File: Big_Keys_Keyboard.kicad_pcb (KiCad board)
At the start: 2 copper layers, 9 parts, among them U1 MX1A-11NN, U2 MX1A-11NN, U3 MX1A-11NN, U4 MX1A-11NN

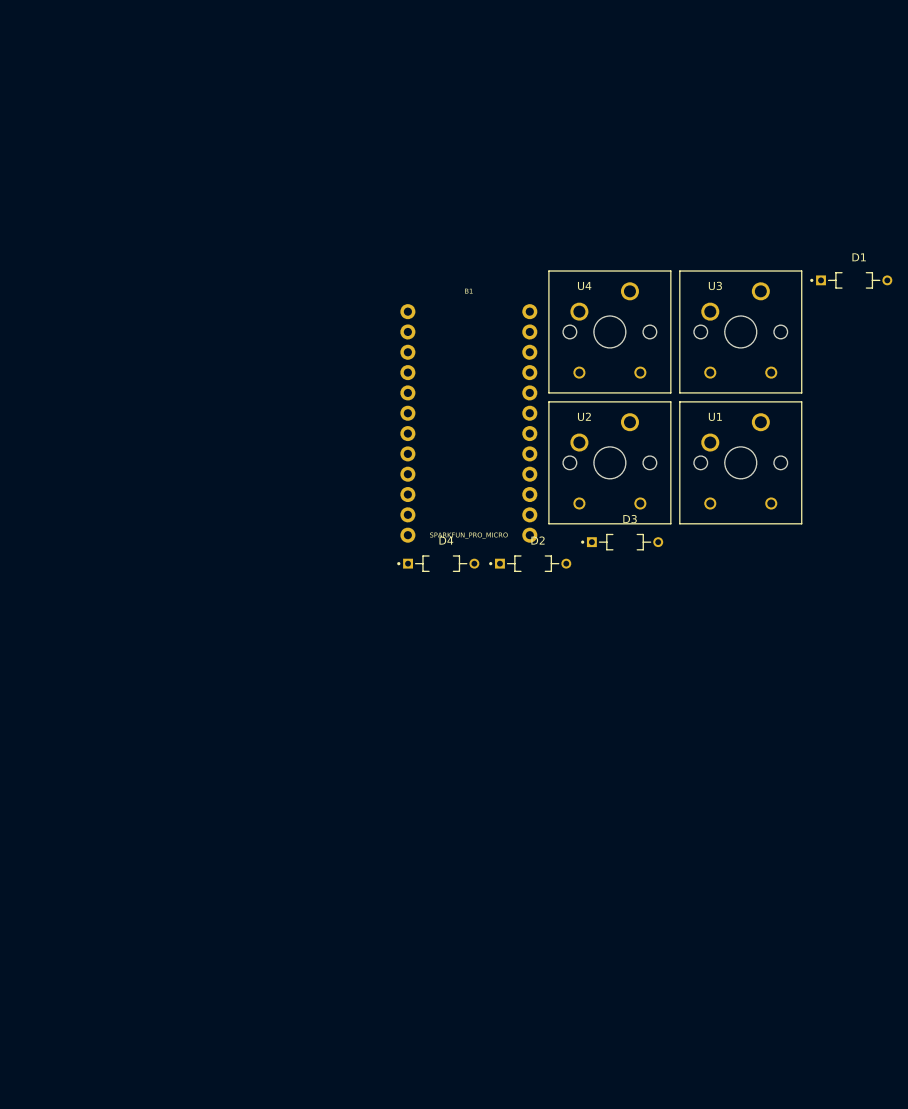
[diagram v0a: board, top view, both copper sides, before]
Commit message: keyboard routes connected in the PCB
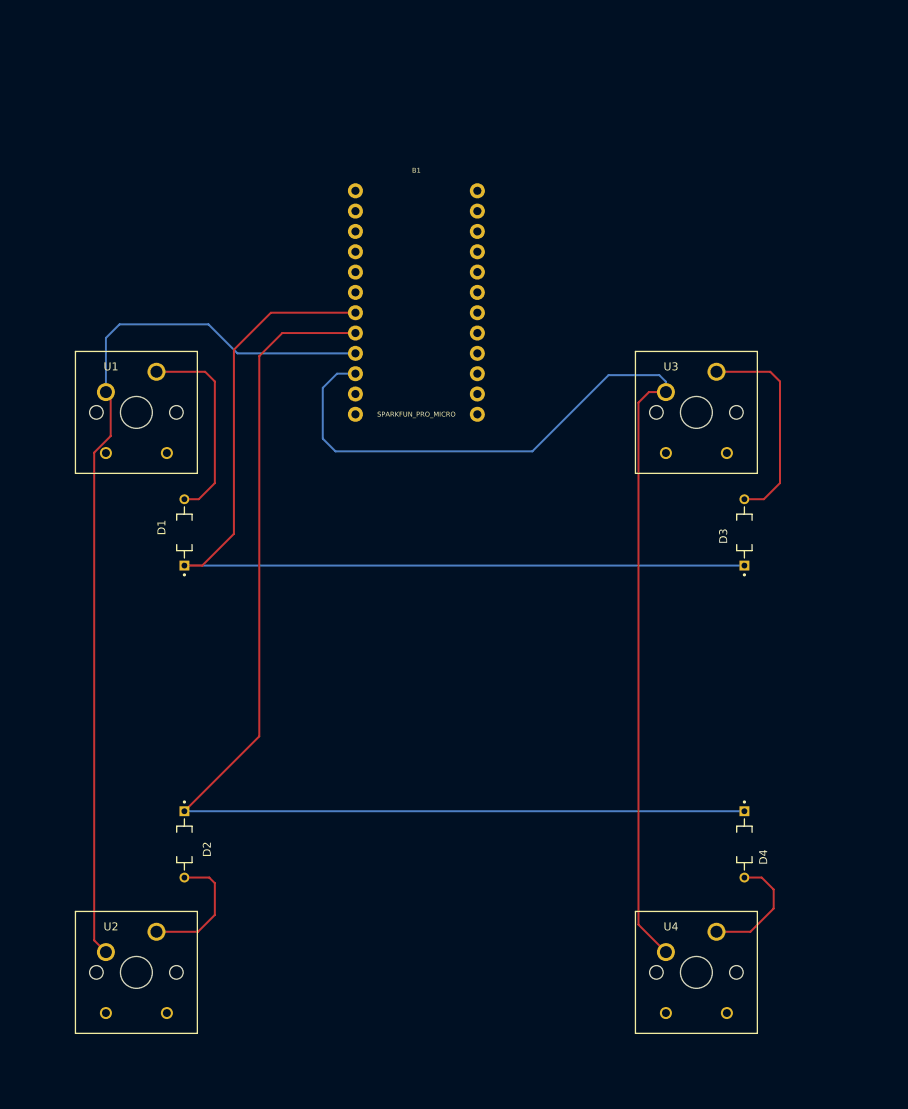
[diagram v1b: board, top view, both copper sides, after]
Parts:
- moved D1 89.5 mm to (97.0, 103.0), turned to 90 degrees
- moved U2 86.9 mm to (91.0, 158.0)
- moved U4 80.8 mm to (161.0, 158.0)
- moved U1 75.8 mm to (91.0, 88.0)
- moved D2 56.0 mm to (97.0, 142.0), turned to -90 degrees
- moved D4 51.6 mm to (167.0, 142.0), turned to -90 degrees
- moved B1 16.5 mm to (126.0, 73.0)
- moved D3 15.0 mm to (167.0, 103.0), turned to 90 degrees
- moved U3 11.5 mm to (161.0, 88.0)
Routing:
- net ROW2: track 0.00 -> 144.0 mm
- net COL2: track 0.00 -> 134.4 mm
- net ROW1: track 0.00 -> 118.0 mm
- net COL1: track 0.00 -> 111.9 mm
- net Net-(D3-PadA): track 0.00 -> 26.4 mm
- net Net-(D1-PadA): track 0.00 -> 25.1 mm
- net Net-(D2-PadA): track 0.00 -> 16.2 mm
- net Net-(D4-PadA): track 0.00 -> 15.0 mm

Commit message: basic pcb for a 4 keyed board ready
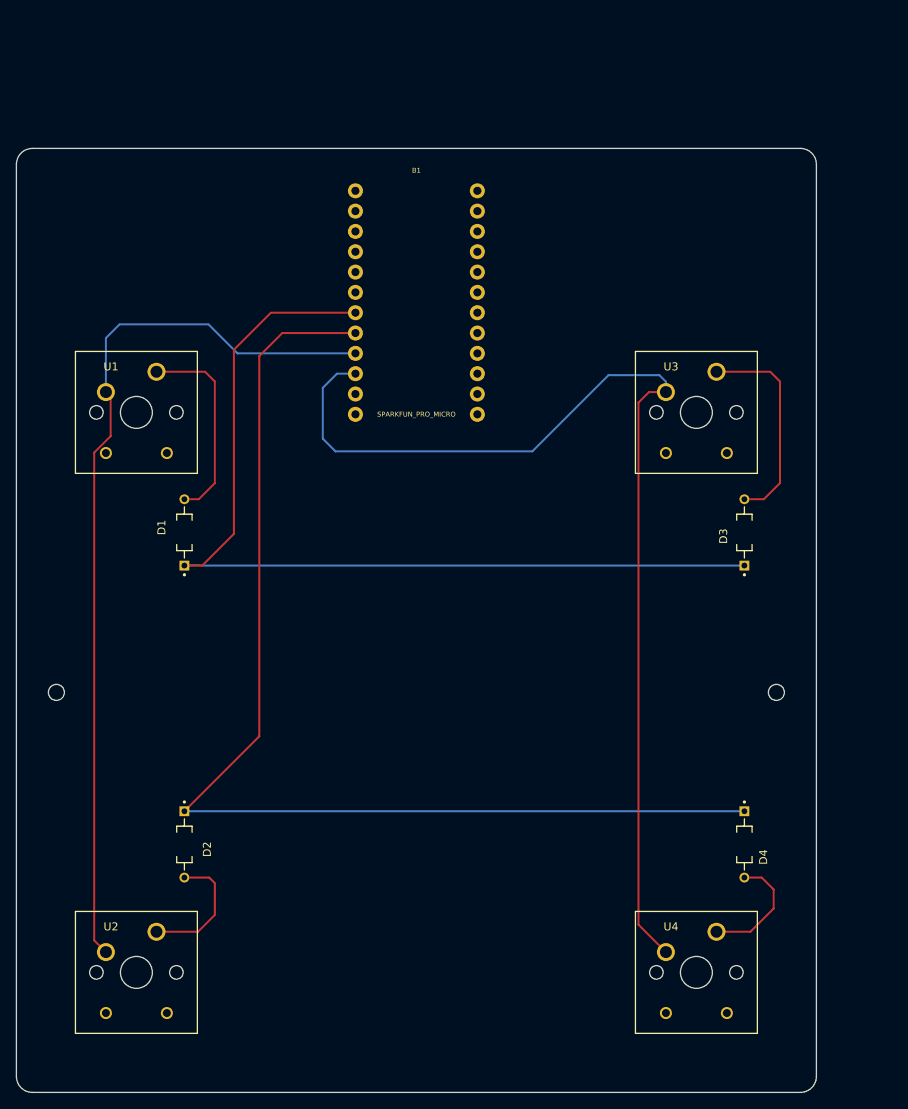
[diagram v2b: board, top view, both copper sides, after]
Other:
- board outline added: 100 x 118 mm
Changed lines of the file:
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@@
       (net 8 "ROW2") (pintype "passive"))
   )
+  (gr_line (start 176 57) (end 176 171) (layer "Edge.Cuts") (width 0.1))
+  (gr_line (start 174 173) (end 78 173) (layer "Edge.Cuts") (width 0.1))
+  (gr_circle (center 81 123) (end 82 123) (layer "Edge.Cuts") (width 0.15) (fill none))
+  (gr_arc (start 76 57) (mid 76.585786 55.585786) (end 78 55) (layer "Edge.Cuts") (width 0.1))
+  (gr_line (start 78 55) (end 174 55) (layer "Edge.Cuts") (width 0.1))
+  (gr_arc (start 176 171) (mid 175.414214 172.414214) (end 174 173) (layer "Edge.Cuts") (width 0.1))
+  (gr_arc (start 78 173) (mid 76.585786 172.414214) (end 76 171) (layer "Edge.Cuts") (width 0.1))
+  (gr_line (start 76 171) (end 76 57) (layer "Edge.Cuts") (width 0.1))
+  (gr_circle (center 171 123) (end 172 123) (layer "Edge.Cuts") (width 0.15) (fill none))
+  (gr_arc (start 174 55) (mid 175.414214 55.585786) (end 176 57) (layer "Edge.Cuts") (width 0.1))
   (segment (start 107.81625 75.54) (end 103.1875 80.16875) (width 0.25) (layer "F.Cu") (net 7))
   (segment (start 103.1875 80.16875) (end 103.1875 103.1875) (width 0.25) (layer "F.Cu") (net 7))
-  (segment (start 118.38 75.54) (end 107.81625 75.54) (width 0.25) (layer "F.Cu") (net 7))
+  (segment (start 118.38 75.54) (end 107.81625 75.54) (width 0.254) (layer "F.Cu") (net 7))
   (segment (start 103.1875 103.1875) (end 99.229 107.146) (width 0.25) (layer "F.Cu") (net 7))
   (segment (start 99.229 107.146) (end 97 107.146) (width 0.25) (layer "F.Cu") (net 7))
-  (segment (start 97 107.146) (end 167 107.146) (width 0.25) (layer "B.Cu") (net 7))
+  (segment (start 97 107.146) (end 167 107.146) (width 0.254) (layer "B.Cu") (net 7))
   (segment (start 106.3625 80.9625) (end 106.3625 128.4915) (width 0.25) (layer "F.Cu") (net 8))
   (segment (start 109.245 78.08) (end 106.3625 80.9625) (width 0.25) (layer "F.Cu") (net 8))
   (segment (start 106.3625 128.4915) (end 97 137.854) (width 0.25) (layer "F.Cu") (net 8))
-  (segment (start 118.38 78.08) (end 109.245 78.08) (width 0.25) (layer "F.Cu") (net 8))
-  (segment (start 97 137.854) (end 167 137.854) (width 0.25) (layer "B.Cu") (net 8))
+  (segment (start 118.38 78.08) (end 109.245 78.08) (width 0.254) (layer "F.Cu") (net 8))
+  (segment (start 97 137.854) (end 167 137.854) (width 0.254) (layer "B.Cu") (net 8))
   (segment (start 87.782717 90.961346) (end 85.725 93.019063) (width 0.25) (layer "F.Cu") (net 9))
   (segment (start 87.782717 86.052717) (end 87.782717 90.961346) (width 0.25) (layer "F.Cu") (net 9))
@@
   (segment (start 85.725 93.019063) (end 85.725 153.995) (width 0.25) (layer "F.Cu") (net 9))
   (segment (start 118.38 80.62) (end 103.63875 80.62) (width 0.25) (layer "B.Cu") (net 9))
-  (segment (start 100.0125 76.99375) (end 88.9 76.99375) (width 0.25) (layer "B.Cu") (net 9))
+  (segment (start 100.0125 76.99375) (end 88.9 76.99375) (width 0.254) (layer "B.Cu") (net 9))
   (segment (start 103.63875 80.62) (end 100.0125 76.99375) (width 0.25) (layer "B.Cu") (net 9))
   (segment (start 88.9 76.99375) (end 87.19 78.70375) (width 0.25) (layer "B.Cu") (net 9))
@@
   (segment (start 140.49375 92.86875) (end 150.01875 83.34375) (width 0.25) (layer "B.Cu") (net 10))
   (segment (start 116.07125 83.16) (end 114.3 84.93125) (width 0.25) (layer "B.Cu") (net 10))
-  (segment (start 99.58875 82.92) (end 100.80625 84.1375) (width 0.25) (layer "F.Cu") (net 25))
+  (segment (start 99.58875 82.92) (end 100.80625 84.1375) (width 0.254) (layer "F.Cu") (net 25))
   (segment (start 100.80625 84.1375) (end 100.80625 96.8375) (width 0.25) (layer "F.Cu") (net 25))
   (segment (start 93.51 82.92) (end 99.58875 82.92) (width 0.25) (layer "F.Cu") (net 25))
   (segment (start 100.80625 96.8375) (end 98.78975 98.854) (width 0.25) (layer "F.Cu") (net 25))
   (segment (start 98.78975 98.854) (end 97 98.854) (width 0.25) (layer "F.Cu") (net 25))
-  (segment (start 100.80625 150.8125) (end 100.80625 146.84375) (width 0.25) (layer "F.Cu") (net 26))
+  (segment (start 100.80625 150.8125) (end 100.80625 146.84375) (width 0.254) (layer "F.Cu") (net 26))
   (segment (start 98.69875 152.92) (end 100.80625 150.8125) (width 0.25) (layer "F.Cu") (net 26))
   (segment (start 93.51 152.92) (end 98.69875 152.92) (width 0.25) (layer "F.Cu") (net 26))
@@
   (segment (start 171.45 84.1375) (end 171.45 96.8375) (width 0.25) (layer "F.Cu") (net 27))
   (segment (start 163.51 82.92) (end 170.2325 82.92) (width 0.25) (layer "F.Cu") (net 27))
-  (segment (start 170.2325 82.92) (end 171.45 84.1375) (width 0.25) (layer "F.Cu") (net 27))
+  (segment (start 170.2325 82.92) (end 171.45 84.1375) (width 0.254) (layer "F.Cu") (net 27))
   (segment (start 167.755 152.92) (end 170.65625 150.01875) (width 0.25) (layer "F.Cu") (net 28))
   (segment (start 169.16475 146.146) (end 167 146.146) (width 0.25) (layer "F.Cu") (net 28))

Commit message: keyboard with all connections done, lack of i2c
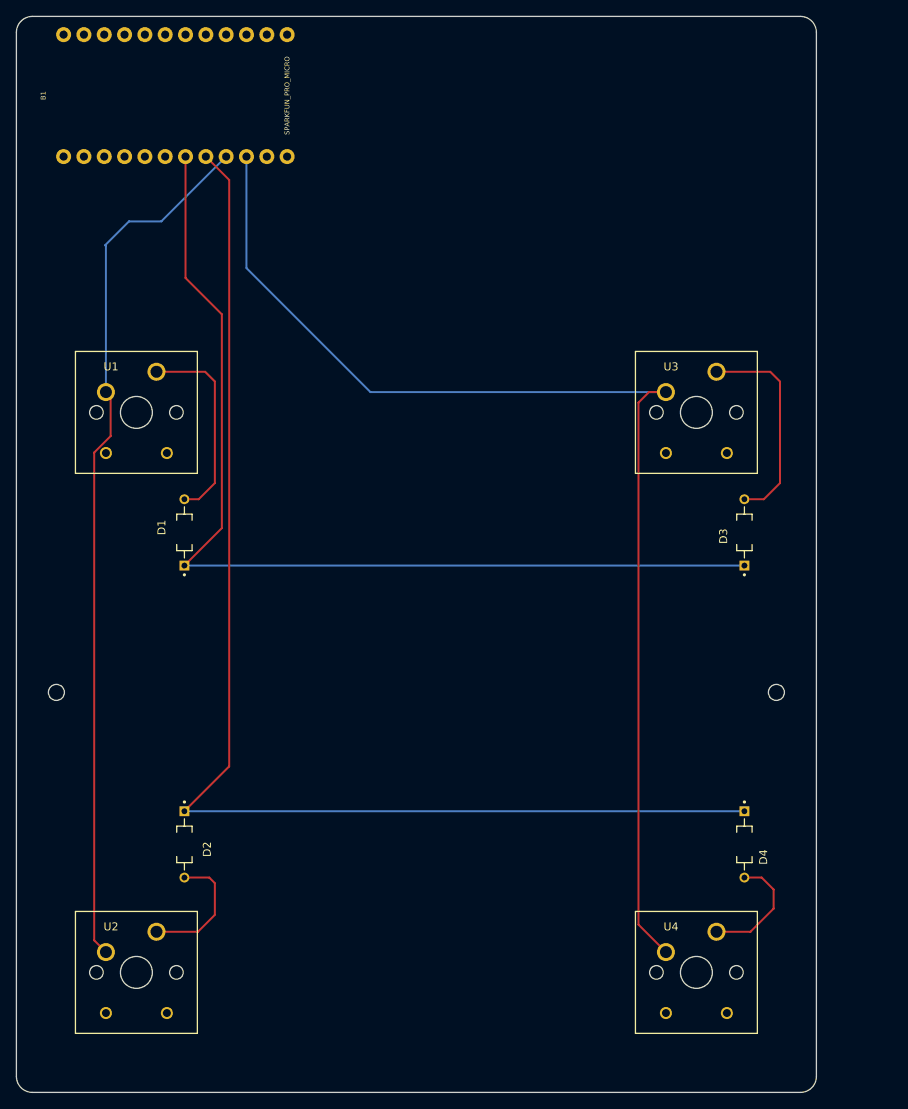
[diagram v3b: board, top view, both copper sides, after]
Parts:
- moved B1 39.9 mm to (94.6, 48.4), turned to 90 degrees
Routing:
- net COL2: track 134.4 -> 146.9 mm
- net ROW2: track 144.0 -> 155.4 mm
- net ROW1: track 118.0 -> 124.9 mm
- net COL1: track 111.9 -> 109.8 mm
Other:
- board size 100 x 118 mm -> 100 x 134.5 mm
